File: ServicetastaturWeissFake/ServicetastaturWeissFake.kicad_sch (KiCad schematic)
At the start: 30 parts, among them J1 Automat, SW1 SW_Push, SW10 SW_Push, SW11 SW_Push, SW12 SW_Push, SW13 SW_Push, SW14 SW_Push, SW15 SW_Push, SW16 SW_Push, SW2 SW_Push, SW3 SW_Push, SW4 SW_Push, SW5 SW_Push, SW6 SW_Push, SW7 SW_Push, SW8 SW_Push, SW9 SW_Push, U1 LTC-4627JD, U2 LTC-4627JD, U3 74LS48, U4 74LS145

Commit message: beschriftung
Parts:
- SW1: value SW_Push -> Ausw.0,10
- SW10: value SW_Push -> Münzung
- SW11: value SW_Push -> ab 0,10
- SW12: value SW_Push -> auf 0,10
- SW13: value SW_Push -> ab Serie
- SW14: value SW_Push -> auf Serie
- SW15: value SW_Push -> ab 1,-
- SW16: value SW_Push -> auf 1,-
- SW2: value SW_Push -> Ausw.1,-
- SW3: value SW_Push -> Ausw.2,-
- SW4: value SW_Push -> Ausw.5,-
- SW5: value SW_Push -> Münzsp.
- SW6: value SW_Push -> Sp.Zähl
- SW7: value SW_Push -> Lampen
- SW8: value SW_Push -> Reset
- SW9: value SW_Push -> Initialisieren
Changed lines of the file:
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@@
 			)
 		)
-		(property "Value" "SW_Push"
+		(property "Value" "ab Serie"
 			(at 147.32 147.32 0)
 			(effects
@@
 		(on_board yes)
 		(dnp no)
-		(fields_autoplaced yes)
 		(property "Reference" "SW11"
-			(at 177.8 144.78 0)
-			(effects
-				(font
-					(size 1.27 1.27)
-				)
-			)
-		)
-		(property "Value" "SW_Push"
+			(at 177.8 145.034 0)
+			(effects
+				(font
+					(size 1.27 1.27)
+				)
+			)
+		)
+		(property "Value" "ab 0,10"
 			(at 177.8 147.32 0)
 			(effects
@@
 			)
 		)
-		(property "Value" "SW_Push"
+		(property "Value" "Ausw.5,-"
 			(at 162.56 134.62 0)
 			(effects
@@
 		(on_board yes)
 		(dnp no)
-		(fields_autoplaced yes)
 		(property "Reference" "SW9"
 			(at 208.28 144.78 0)
@@
 			)
 		)
-		(property "Value" "SW_Push"
+		(property "Value" "Initialisieren"
 			(at 208.28 147.32 0)
 			(effects
@@
 			)
 		)
-		(property "Value" "SW_Push"
+		(property "Value" "Ausw.1,-"
 			(at 193.04 134.62 0)
 			(effects
@@
 			)
 		)
-		(property "Value" "SW_Push"
+		(property "Value" "Münzsp."
 			(at 147.32 134.62 0)
 			(effects
@@
 			)
 		)
-		(property "Value" "SW_Push"
+		(property "Value" "Sp.Zähl"
 			(at 132.08 134.62 0)
 			(effects
@@
 			)
 		)
-		(property "Value" "SW_Push"
+		(property "Value" "Ausw.2,-"
 			(at 177.8 134.62 0)
 			(effects
@@
 			)
 		)
-		(property "Value" "SW_Push"
+		(property "Value" "Lampen"
 			(at 116.84 134.62 0)
 			(effects
@@
 			)
 		)
-		(property "Value" "SW_Push"
+		(property "Value" "auf 0,10"
 			(at 162.56 147.32 0)
 			(effects
@@
 			)
 		)
-		(property "Value" "SW_Push"
+		(property "Value" "Münzung"
 			(at 193.04 147.32 0)
 			(effects
@@
 			)
 		)
-		(property "Value" "SW_Push"
+		(property "Value" "Reset"
 			(at 101.6 134.62 0)
 			(effects
@@
 			)
 		)
-		(property "Value" "SW_Push"
+		(property "Value" "auf Serie"
 			(at 132.08 147.32 0)
 			(effects
@@
 			)
 		)
-		(property "Value" "SW_Push"
+		(property "Value" "ab 1,-"
 			(at 116.84 147.32 0)
 			(effects
@@
 			)
 		)
-		(property "Value" "SW_Push"
+		(property "Value" "auf 1,-"
 			(at 101.6 147.32 0)
 			(effects
@@
 			)
 		)
-		(property "Value" "SW_Push"
+		(property "Value" "Ausw.0,10"
 			(at 208.28 134.62 0)
 			(effects

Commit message: CC redesign
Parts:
- removed U1, U2: LTC-4627JD, Display_7Segment:LTC-4627Jx, symbol Display_Character:LTC-4627JD
- added C1, C2: C, Capacitor_THT:C_Disc_D4.3mm_W1.9mm_P5.00mm, symbol Device:C
- added C3, C4: C, Capacitor_SMD:C_0805_2012Metric, symbol Device:C
- added D3: LED, LED_THT:LED_D5.0mm, symbol Device:LED
- added H1, H2: MountingHole, MountingHole:MountingHole_3.2mm_M3, symbol Mechanical:MountingHole
- added R10, R11, R12, R13, R14, R15, R16, R17, R18: 470 Ω, Resistor_SMD:R_0805_2012Metric, symbol Device:R
- added R8, R9: 470 Ω, Resistor_THT:R_Axial_DIN0207_L6.3mm_D2.5mm_P7.62mm_Horizontal, symbol Device:R
- added SW17: ↙0,10, Button_Switch_THT:SW_PUSH_6mm, symbol Switch:SW_Push
- added SW18: ↙1,-, Button_Switch_THT:SW_PUSH_6mm, symbol Switch:SW_Push
- added SW19: Auszahlquote, Button_Switch_THT:SW_PUSH_6mm, symbol Switch:SW_Push
- added SW20: ↙5,-, Button_Switch_THT:SW_PUSH_6mm, symbol Switch:SW_Push
- added SW21: Münzsp., Button_Switch_THT:SW_PUSH_6mm, symbol Switch:SW_Push
- added SW22: Sp.Zähl, Button_Switch_THT:SW_PUSH_6mm, symbol Switch:SW_Push
- added SW23: Lampen, Button_Switch_THT:SW_PUSH_6mm, symbol Switch:SW_Push
- added SW24: Reset, Button_Switch_THT:SW_PUSH_6mm, symbol Switch:SW_Push
- added SW25: Initialisieren, Button_Switch_THT:SW_PUSH_6mm, symbol Switch:SW_Push
- added SW26: Münzung, Button_Switch_THT:SW_PUSH_6mm, symbol Switch:SW_Push
- added SW27: Ende, Button_Switch_THT:SW_PUSH_6mm, symbol Switch:SW_Push
- added SW28: ↑0,10, Button_Switch_THT:SW_PUSH_6mm, symbol Switch:SW_Push
- added SW29: ↓Serie, Button_Switch_THT:SW_PUSH_6mm, symbol Switch:SW_Push
- added SW30: ↑Serie, Button_Switch_THT:SW_PUSH_6mm, symbol Switch:SW_Push
- added SW31: ↓1,-, Button_Switch_THT:SW_PUSH_6mm, symbol Switch:SW_Push
- added SW32: ↑1,-, Button_Switch_THT:SW_PUSH_6mm, symbol Switch:SW_Push
- added U1, U2: CC56-12CGKWA, Display_7Segment:CA56-12CGKWA, symbol Display_Character:CC56-12CGKWA
- R1, R2, R3, R4, R5, R6, R7: footprint Resistor_THT:R_Axial_DIN0207_L6.3mm_D2.5mm_P10.16mm_Horizontal -> Resistor_THT:R_Axial_DIN0207_L6.3mm_D2.5mm_P7.62mm_Horizontal
- SW1: value Ausw.0,10 -> Gewinn; footprint Button_Switch_THT:SW_PUSH_6mm -> Button_Switch_THT:SW_PUSH-12mm
- SW10: value Münzung -> Lautspr./; footprint Button_Switch_THT:SW_PUSH_6mm -> Button_Switch_THT:SW_PUSH-12mm
- SW11: value ab 0,10 -> ↓0,10; footprint Button_Switch_THT:SW_PUSH_6mm -> Button_Switch_THT:SW_PUSH-12mm
- SW12: value auf 0,10 -> ↑0,10; footprint Button_Switch_THT:SW_PUSH_6mm -> Button_Switch_THT:SW_PUSH-12mm
- SW13: value ab Serie -> ↓Serie; footprint Button_Switch_THT:SW_PUSH_6mm -> Button_Switch_THT:SW_PUSH-12mm
- SW14: value auf Serie -> ↑Serie; footprint Button_Switch_THT:SW_PUSH_6mm -> Button_Switch_THT:SW_PUSH-12mm
- SW15: value ab 1,- -> Zeit; footprint Button_Switch_THT:SW_PUSH_6mm -> Button_Switch_THT:SW_PUSH-12mm
- SW16: value auf 1,- -> ↑1,-; footprint Button_Switch_THT:SW_PUSH_6mm -> Button_Switch_THT:SW_PUSH-12mm
- SW2: value Ausw.1,- -> Foul; footprint Button_Switch_THT:SW_PUSH_6mm -> Button_Switch_THT:SW_PUSH-12mm
- SW3: value Ausw.2,- -> ↙2,-; footprint Button_Switch_THT:SW_PUSH_6mm -> Button_Switch_THT:SW_PUSH-12mm
- SW4: value Ausw.5,- -> HW-Test; footprint Button_Switch_THT:SW_PUSH_6mm -> Button_Switch_THT:SW_PUSH-12mm
- SW5, SW6, SW8, SW9: footprint Button_Switch_THT:SW_PUSH_6mm -> Button_Switch_THT:SW_PUSH-12mm
- SW7: value Lampen -> Dauerlauf; footprint Button_Switch_THT:SW_PUSH_6mm -> Button_Switch_THT:SW_PUSH-12mm
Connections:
- net +5V: now also C1.1, C2.1, C3.1, C4.1, R17.1, R18.1, R8.1, R9.1
- net GND: now also C1.2, C2.2, C3.2, C4.2, D3.1 (K)
- net TS0: now also SW17.2, SW25.2
- net TS1: now also SW18.2, SW26.2
- net TS2: now also SW19.2, SW27.2
- net TS3: now also SW20.2, SW28.2
- net TS4: now also SW21.2, SW29.2
- net TS5: now also SW22.2, SW30.2
- net TS6: now also SW23.2, SW31.2
- net TS7: now also SW24.2, SW32.2
- net at D1.1 (K), SW10.1, SW11.1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: now also SW25.1, SW26.1, SW27.1, SW28.1, SW29.1, SW30.1, SW31.1, SW32.1
- net at R2.1, U3.12 (b): now also R11.1
- net at R2.2: now also R11.2, U1.7 (b), U2.7 (b)
- net at R4.1, U3.10 (d): now also R13.1
- net at R4.2: now also R13.2, U1.2 (d), U2.2 (d)
- net at D2.1 (K), SW1.1, SW2.1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: now also SW17.1, SW18.1, SW19.1, SW20.1, SW21.1, SW22.1, SW23.1, SW24.1
- net at R3.1, U3.11 (c): now also R12.1
- net at R3.2: now also R12.2, U1.4 (c), U2.4 (c)
- net at R5.1, U3.9 (e): now also R14.1
- net at R5.2: now also R14.2, U1.1 (e), U2.1 (e)
- net at U4.1 (Q0): now also U1.12 (CC1)
- net at U4.2 (Q1): now also U1.9 (CC2)
- net at U4.3 (Q2): now also U1.8 (CC3)
- net at U4.4 (Q3): now also U1.6 (CC4)
- net at U4.5 (Q4): now also U2.12 (CC1)
- net at U4.6 (Q5): now also U2.9 (CC2)
- net at U4.7 (Q6): now also U2.8 (CC3)
- net at U4.9 (Q7): now also U2.6 (CC4)
- net at R6.2: now also R15.2, U1.10 (f), U2.10 (f)
- net at R1.2: now also R10.2, U1.11 (a), U2.11 (a)
- net at R7.2: now also R16.2, U1.5 (g), U2.5 (g)
- net at R6.1, U3.15 (f): now also R15.1
- net at R1.1, U3.13 (a): now also R10.1
- net at R7.1, U3.14 (g): now also R16.1
- new net: R17.2, R8.2, U1.3 (DPX), U2.3 (DPX)
- new net: D3.2 (A), R18.2, R9.2
- no-connect marks 6 -> 2
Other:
- moved on the sheet: U4

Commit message: led
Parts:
- added D4: LED, LED_SMD:LED_0805_2012Metric, symbol Device:LED
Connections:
- net GND: now also D4.1 (K)
- net at D3.2 (A), R18.2, R9.2: now also D4.2 (A)
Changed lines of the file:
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@@
+	)
+	(junction
+		(at 87.63 30.48)
+		(diameter 0)
+		(color 0 0 0 0)
 	)
 	(junction
@@
 					(unit 1)
 				)
+			)
+		)
+	)
+	(symbol
+		(lib_id "Device:LED")
+		(at 83.82 30.48 180)
+		(unit 1)
+		(exclude_from_sim no)
+		(in_bom yes)
+		(on_board yes)
+		(dnp no)
+		(fields_autoplaced yes)
+		(property "Reference" "D4"
+			(at 85.4075 22.86 0)
+			(effects
+				(font
+					(size 1.27 1.27)
+				)
+			)
+		)
+		(property "Value" "LED"
+			(at 85.4075 25.4 0)
+			(effects
+				(font
+					(size 1.27 1.27)
+				)
+			)
+		)
+		(property "Footprint" "LED_SMD:LED_0805_2012Metric"
+			(at 83.82 30.48 0)
+			(effects
+				(font
+					(size 1.27 1.27)
+				)
+				(hide yes)
+			)
+		)
+		(property "Datasheet" "~"
+			(at 83.82 30.48 0)
+			(effects
+				(font
+					(size 1.27 1.27)
+				)
+				(hide yes)
+			)
+		)
+		(property "Description" "Light emitting diode"
+			(at 83.82 30.48 0)
+			(effects
+				(font
+					(size 1.27 1.27)
+				)
+				(hide yes)
+			)
+		)
+		(pin "2"
+		)
+		(pin "1"
+		)
+		(instances
+			(project "ServicetastaturWeissFake"
+				(path "/c7f9b05e-617f-48d9-bed2-6de097771a4c"
+					(reference "D4")
+					(unit 1)
+				)

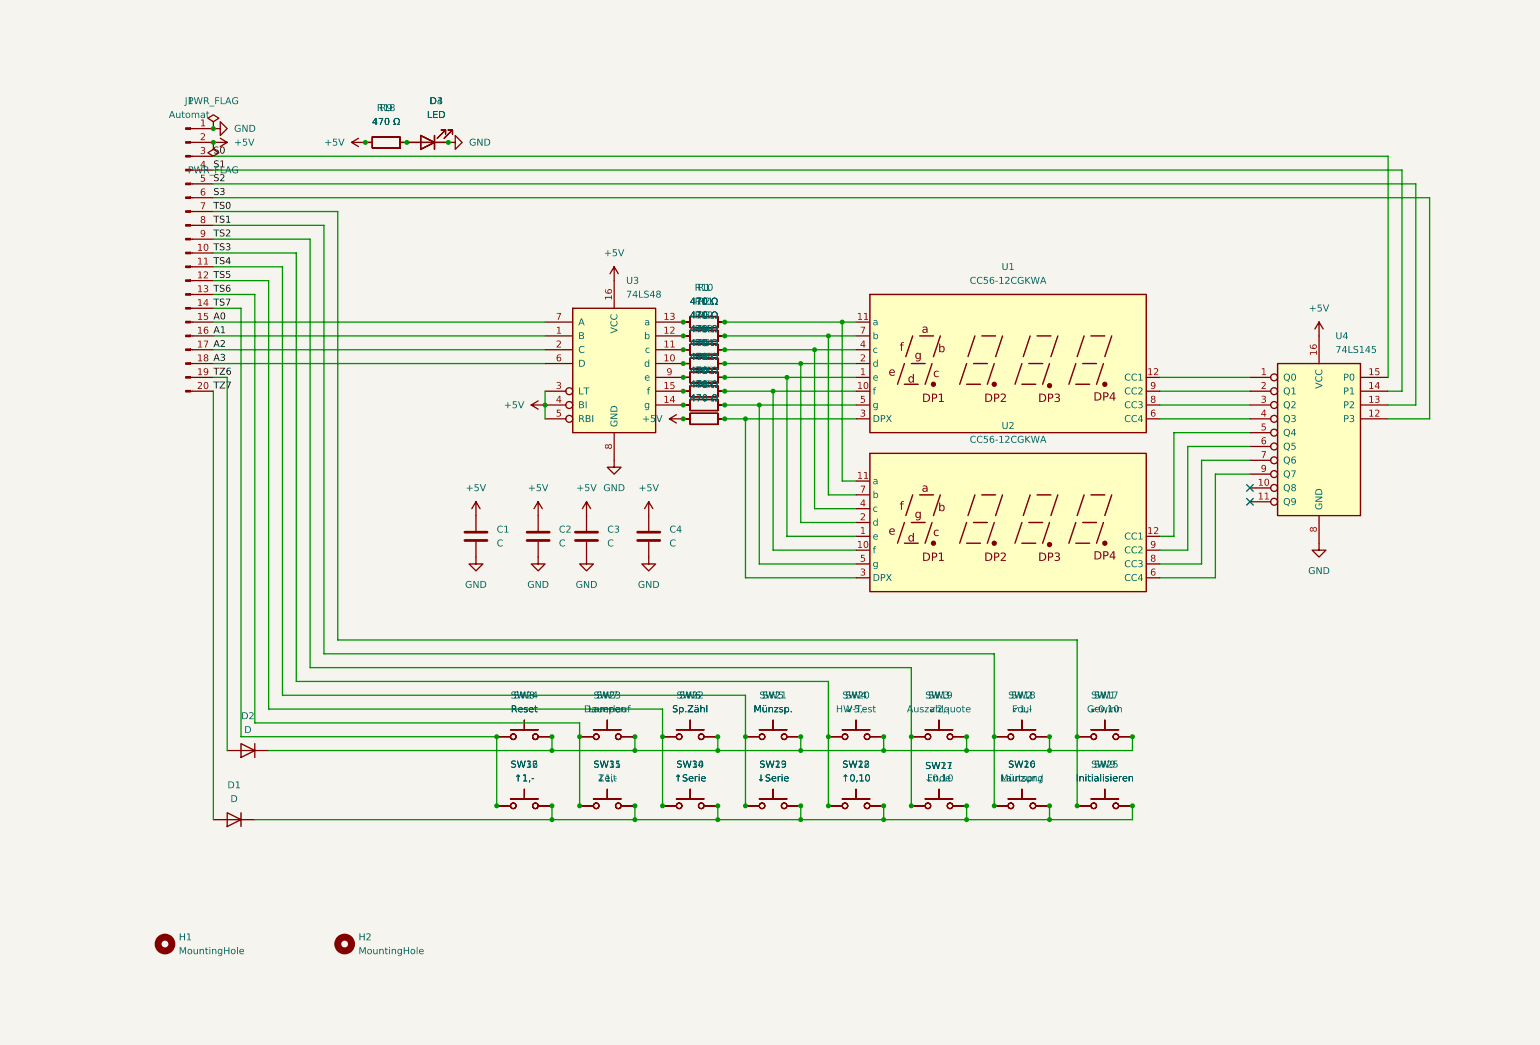
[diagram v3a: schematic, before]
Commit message: b3f schalter und displays gedreht
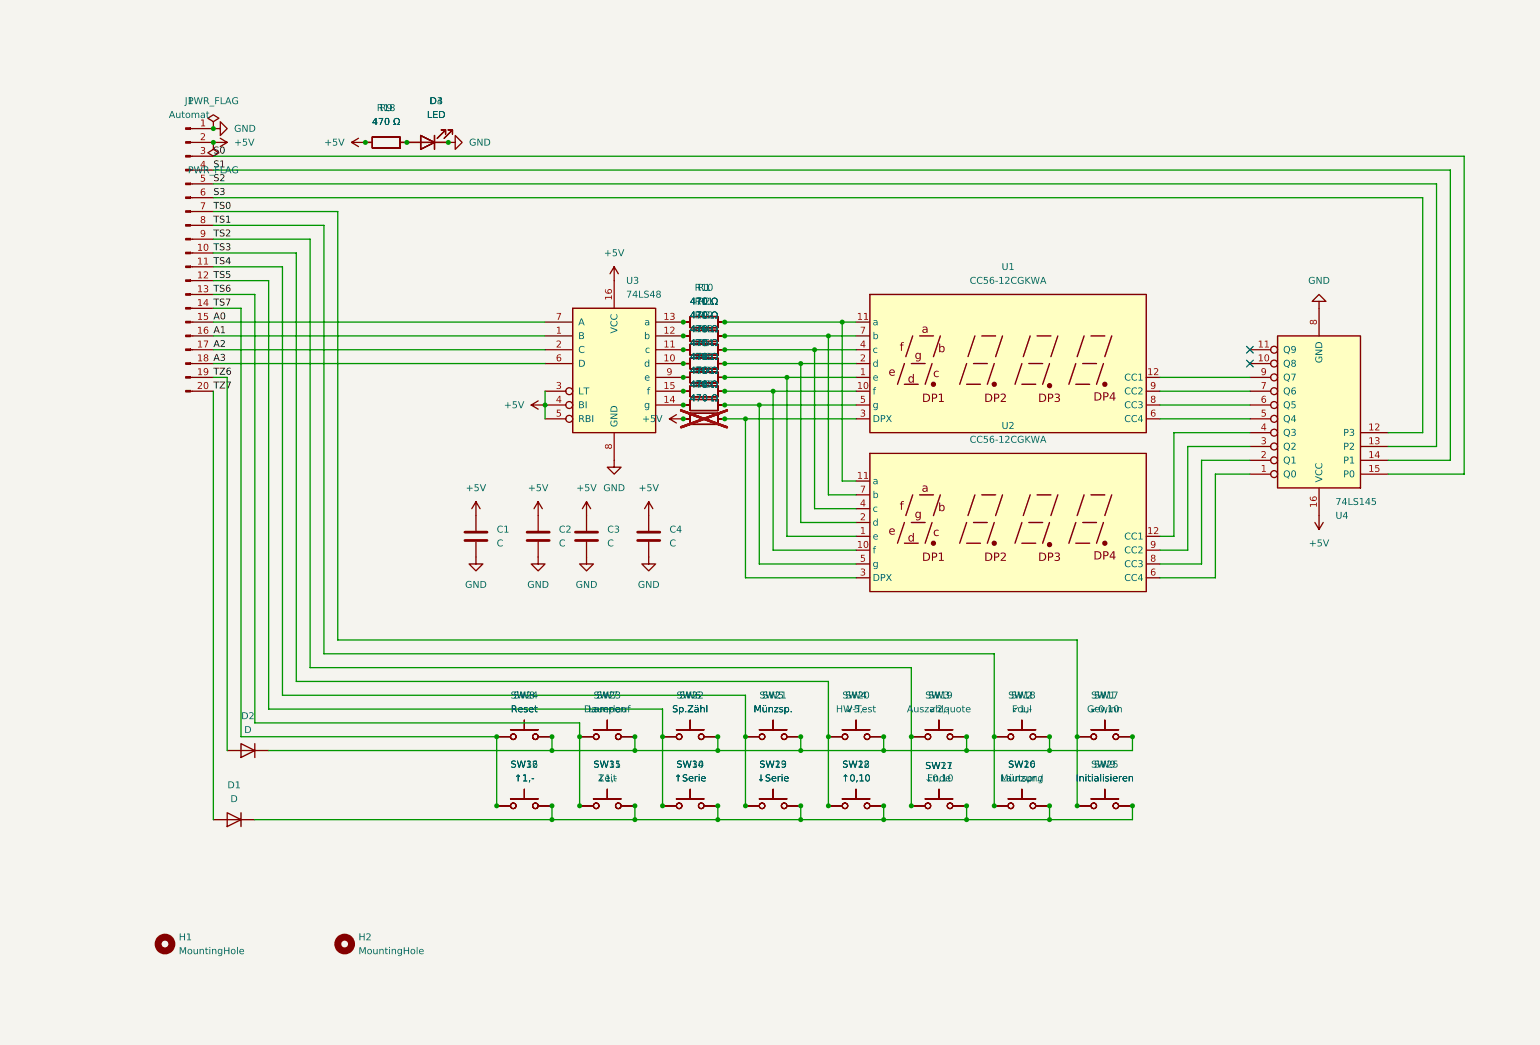
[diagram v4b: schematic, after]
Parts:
- R17, R8: now not fitted
- SW1, SW10, SW11, SW12, SW13, SW14, SW15, SW16, SW2, SW3, SW4, SW5, SW6, SW7, SW8, SW9: footprint Button_Switch_THT:SW_PUSH-12mm -> Button_Switch_THT:SW_SPST_Omron_B3F-40xx
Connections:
- net at U1.12 (CC1): now also U4.9 (Q7); no longer U4.1 (Q0)
- net at U1.6 (CC4): now also U4.5 (Q4); no longer U4.4 (Q3)
- net at U1.8 (CC3): now also U4.6 (Q5); no longer U4.3 (Q2)
- net at U1.9 (CC2): now also U4.7 (Q6); no longer U4.2 (Q1)
- net at U2.12 (CC1): now also U4.4 (Q3); no longer U4.5 (Q4)
- net at U2.9 (CC2): now also U4.3 (Q2); no longer U4.6 (Q5)
- net at U2.8 (CC3): now also U4.2 (Q1); no longer U4.7 (Q6)
- net at U2.6 (CC4): now also U4.1 (Q0); no longer U4.9 (Q7)
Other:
- moved on the sheet: U4

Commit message: doppelIC
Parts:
- added JP1: Jumper_3_Bridged12, Jumper:SolderJumper-3_P1.3mm_Bridged12_Pad1.0x1.5mm_NumberLabels, symbol Jumper:Jumper_3_Bridged12
- added U5: 74LS48, Package_SO:SOIC-16_4.55x10.3mm_P1.27mm, symbol 74xx:74LS48
- added U6: 74LS145, Package_SO:SOIC-16_4.55x10.3mm_P1.27mm, symbol 74xx:74LS145
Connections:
- net +5V: now also JP1.3 (B), U5.16 (VCC), U5.3 (LT), U5.5 (RBI), U6.16 (VCC); no longer U3.4 (BI)
- net A0: now also U5.7 (A)
- net A1: now also U5.1 (B)
- net A2: now also U5.2 (C)
- net A3: now also U5.6 (D)
- net GND: now also U5.8 (GND), U6.8 (GND)
- net S0: now also U6.15 (P0)
- net S1: now also U6.14 (P1)
- net S2: now also U6.13 (P2)
- net S3: now also U6.12 (P3)
- net at U1.12 (CC1), U4.9 (Q7): now also U6.9 (Q7)
- net at U1.6 (CC4), U4.5 (Q4): now also U6.5 (Q4)
- net at U1.8 (CC3), U4.6 (Q5): now also U6.6 (Q5)
- net at U1.9 (CC2), U4.7 (Q6): now also U6.7 (Q6)
- net at R15.1, R6.1, U3.15 (f): now also U5.15 (f)
- net at R13.1, R4.1, U3.10 (d): now also U5.10 (d)
- net at R11.1, R2.1, U3.12 (b): now also U5.12 (b)
- net at R12.1, R3.1, U3.11 (c): now also U5.11 (c)
- net at R16.1, R7.1, U3.14 (g): now also U5.14 (g)
- net at R1.1, R10.1, U3.13 (a): now also U5.13 (a)
- net at R14.1, R5.1, U3.9 (e): now also U5.9 (e)
- net at U2.6 (CC4), U4.1 (Q0): now also U6.1 (Q0)
- net at U4.10 (Q8): now also U4.11 (Q9), JP1.1 (A), U6.10 (Q8), U6.11 (Q9)
- net at U2.8 (CC3), U4.2 (Q1): now also U6.2 (Q1)
- net at U2.9 (CC2), U4.3 (Q2): now also U6.3 (Q2)
- net at U2.12 (CC1), U4.4 (Q3): now also U6.4 (Q3)
- new net: JP1.2 (C), U3.4 (BI), U5.4 (BI)
- no-connect marks 2 -> 0

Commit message: kleine LED
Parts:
- D3: footprint LED_THT:LED_D5.0mm -> LED_THT:LED_D3.0mm
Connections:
- net at U1.3 (DPX), U2.3 (DPX): no longer R17.2, R8.2
- new net: R17.2, R8.2
- no-connect marks 0 -> 1
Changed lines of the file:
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@@
 	)
 	(junction
-		(at 234.95 88.9)
+		(at 138.43 81.28)
 		(diameter 0)
 		(color 0 0 0 0)
 	)
 	(junction
-		(at 172.72 139.7)
+		(at 234.95 88.9)
 		(diameter 0)
 		(color 0 0 0 0)
 	)
 	(junction
-		(at 203.2 139.7)
+		(at 172.72 139.7)
 		(diameter 0)
 		(color 0 0 0 0)
 	)
 	(junction
-		(at 142.24 81.28)
+		(at 203.2 139.7)
 		(diameter 0)
 		(color 0 0 0 0)
@@
 	)
 	(junction
-		(at 138.43 81.28)
-		(diameter 0)
-		(color 0 0 0 0)
-	)
-	(junction
 		(at 154.94 68.58)
 		(diameter 0)
@@
 		(color 0 0 0 0)
 	)
-	(wire
-		(pts
-			(xy 142.24 110.49) (xy 142.24 81.28)
-		)
-		(stroke
-			(width 0)
-			(type default)
-		)
+	(no_connect
+		(at 139.7 81.28)
 	)
 	(wire
@@
 	(wire
 		(pts
-			(xy 218.44 73.66) (xy 234.95 73.66)
+			(xy 142.24 110.49) (xy 142.24 81.28)
 		)
 		(stroke
@@
 	(wire
 		(pts
-			(xy 226.06 88.9) (xy 226.06 107.95)
+			(xy 218.44 73.66) (xy 234.95 73.66)
 		)
 		(stroke
@@
 	(wire
 		(pts
-			(xy 138.43 81.28) (xy 142.24 81.28)
+			(xy 226.06 88.9) (xy 226.06 107.95)
 		)
 		(stroke
@@
 	(wire
 		(pts
-			(xy 162.56 110.49) (xy 142.24 110.49)
-		)
-		(stroke
-			(width 0)
-			(type default)
-		)
-	)
-	(wire
-		(pts
 			(xy 172.72 152.4) (xy 172.72 139.7)
 		)
@@
 	(wire
 		(pts
+			(xy 162.56 110.49) (xy 142.24 110.49)
+		)
+		(stroke
+			(width 0)
+			(type default)
+		)
+	)
+	(wire
+		(pts
 			(xy 96.52 152.4) (xy 96.52 139.7)
 		)
@@
 	(wire
 		(pts
+			(xy 138.43 81.28) (xy 139.7 81.28)
+		)
+		(stroke
+			(width 0)
+			(type default)
+		)
+	)
+	(wire
+		(pts
 			(xy 137.16 152.4) (xy 137.16 154.94)
 		)
@@
 	(wire
 		(pts
-			(xy 142.24 81.28) (xy 162.56 81.28)
-		)
-		(stroke
-			(width 0)
-			(type default)
-		)
-	)
-	(wire
-		(pts
 			(xy 138.43 63.5) (xy 160.02 63.5)
 		)
@@
 	(wire
 		(pts
+			(xy 142.24 81.28) (xy 162.56 81.28)
+		)
+		(stroke
+			(width 0)
+			(type default)
+		)
+	)
+	(wire
+		(pts
 			(xy 187.96 124.46) (xy 64.77 124.46)
 		)
@@
 			)
 		)
-		(property "Footprint" "LED_THT:LED_D5.0mm"
+		(property "Footprint" "LED_THT:LED_D3.0mm"
 			(at 83.82 30.48 0)
 			(effects
